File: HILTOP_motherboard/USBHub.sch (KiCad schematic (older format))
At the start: 64 parts, among them U2 TPS2044B, U3 TUSB2077A, U4 SN75240PWR, U6 SN75240PWR, Y1 6MHz Crystal

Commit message: Added new USB2.0 device
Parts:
- removed C28, C29, C36, C37, C38, C39, C40, C41, C42, C43, C44, C45, C46, C47, C48, C49: 22pF, Capacitors_SMD:C_0603, symbol C
- removed C31, C34: 100nF, Capacitors_SMD:C_0603, symbol C
- removed R18, R19, R23, R24, R29, R30, R34, R35, R36, R37, R40, R41, R42, R43, R46, R47: 27R, Resistors_SMD:R_0603, symbol R
- removed R22: 1.5K, Resistors_SMD:R_0603, symbol R
- removed R25, R26, R32, R33, R38, R39, R44, R45, R48, R49, R50, R51, R52, R53: 15K, Resistors_SMD:R_0603, symbol R
- removed R28, R31: 10K, Resistors_SMD:R_0603, symbol R
- removed U2: TPS2044B, Housings_SOIC:SOIC-16_3.9x9.9mm_Pitch1.27mm, symbol TPS2044B
- removed U3: TUSB2077A, Housings_QFP:LQFP-48_7x7mm_Pitch0.5mm, symbol TUSB2077A
- removed U4, U6: SN75240PWR, Housings_SSOP:TSSOP-8_4.4x3mm_Pitch0.65mm, symbol SN75240PWR
- added C? (x9): 100nF, Capacitors_SMD:C_0603, symbol C
- added C? (x4): 1uF, Capacitors_SMD:C_0603, symbol C
- added D? (x7): GRN, symbol LED
- added D? (x7): YEL, symbol LED
- added D? (x3): RED, symbol LED
- added R? (x6): 10K, Resistors_SMD:R_0603, symbol R
- added R? (x3): DNF, Resistors_SMD:R_0603, symbol R
- added R? (x17): 330R, Resistors_SMD:R_0603, symbol R
- added U3, U?: USB2517, MODULE, symbol USB2517
- added U? (x2): MIC2026-1YM, MODULE, symbol MIC2026-1YM
- C32: value 1nF -> 100nF; Devtank 106-004 -> 105-002
- R20: value 10K -> 100K; Devtank 101-010 -> 101-015
- R21: value 1.5K -> 1M; Devtank 101-032 -> 101-019
- R27: value 10K -> 12K; Devtank 101-010 -> 101-044
- Y1: value 6MHz Crystal -> 24MHz Crystal; Devtank 181-002 -> 181-003
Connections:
- net labels added: OCS1, OCS2, OCS4, PWR1_5V, PWR2_5V, PWR4_5V, USB1_EN, USB4_EN
- net labels removed: D2_5V, D3_5V, D6_5V, D7_5V, USB0_N, USB0_P, USB2_OC, USB3_EN, USB3_OC, USB6_EN, USB6_OC, USB7_EN, USB7_OC, USB_CFG_OK, USB_PORTDIS, USB_PORTPWR
- wire segments 240 -> 195
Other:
- note added: "Default Config - 101\nInternal Defaults\nDynamic Power (local)\nUSB LED Mode"
- note added: "Over-current Monitoring on external ports only"
- moved on the sheet: C30, C32, C33, C35, R152, R20, R21, R27, Y1

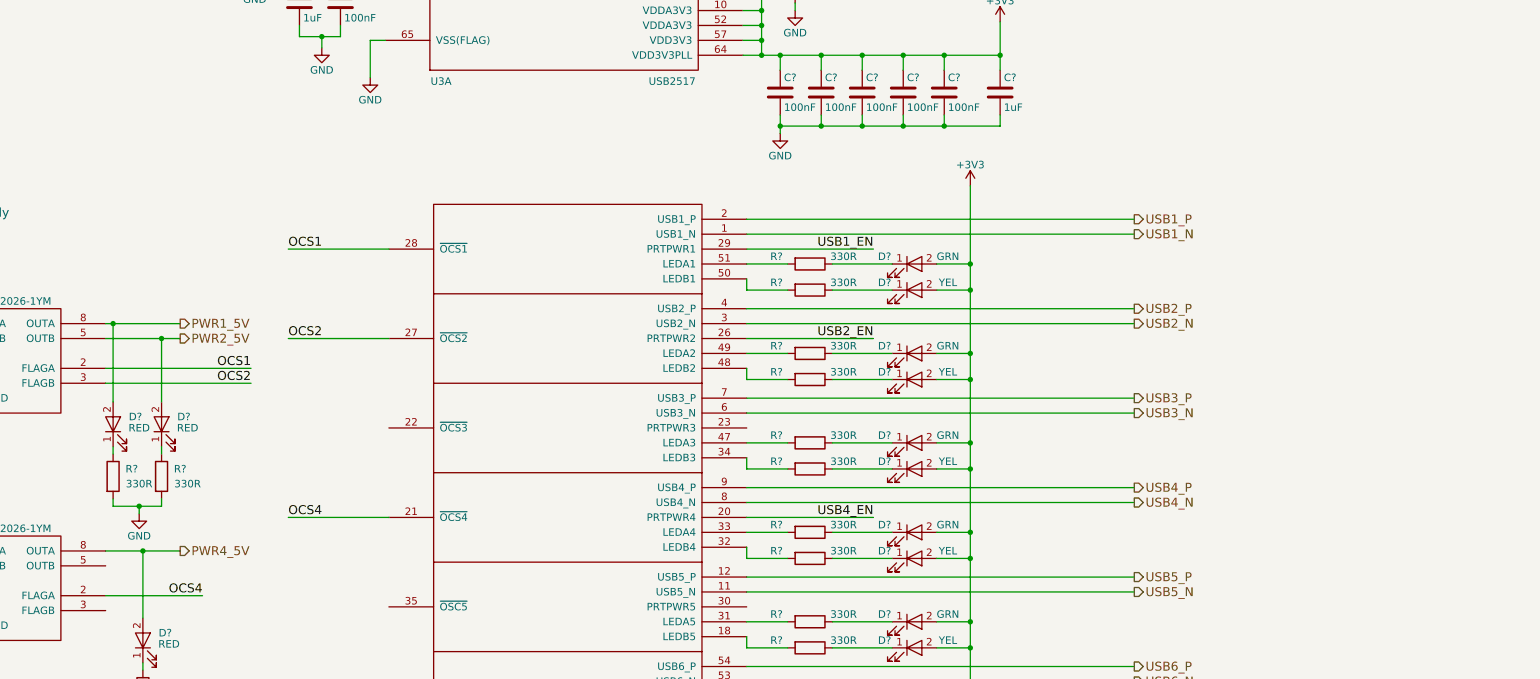
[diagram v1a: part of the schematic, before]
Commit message: add SP3003 ESD protection diodes to USB circuit
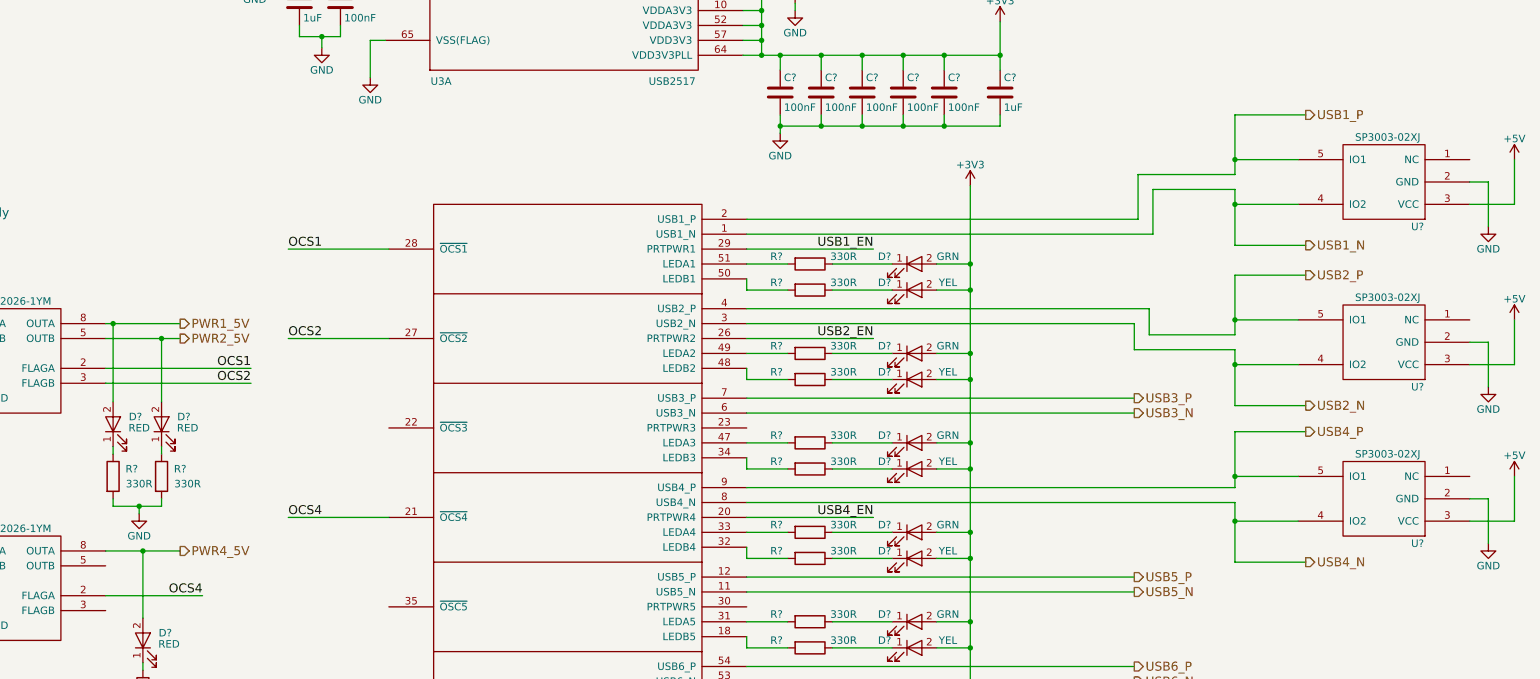
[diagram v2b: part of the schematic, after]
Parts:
- added U? (x3): SP3003-02XJ, Devtank_PCB_Lib:SC70-5, symbol SP3003-02XJ
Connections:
- net +5V: now also U?.3 (VCC), U?.3 (VCC), U?.3 (VCC)
- net GND: now also U?.2 (GND), U?.2 (GND), U?.2 (GND)
- net USB1_N: now also U?.4 (IO2)
- net USB1_P: now also U?.5 (IO1)
- net USB2_N: now also U?.4 (IO2)
- net USB2_P: now also U?.5 (IO1)
- net USB4_N: now also U?.4 (IO2)
- net USB4_P: now also U?.5 (IO1)

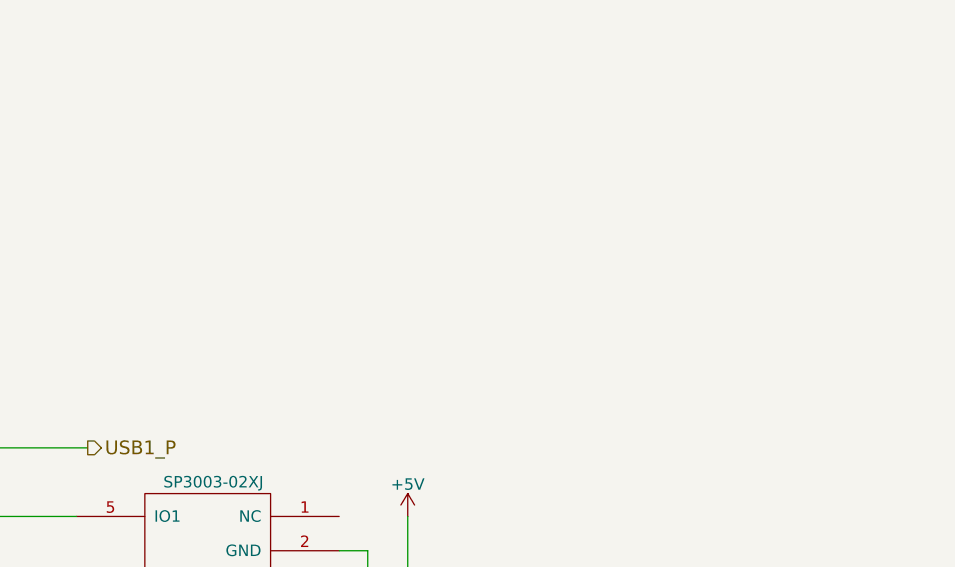
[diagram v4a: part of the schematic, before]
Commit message: Fixed giabit LAN Schematic errors
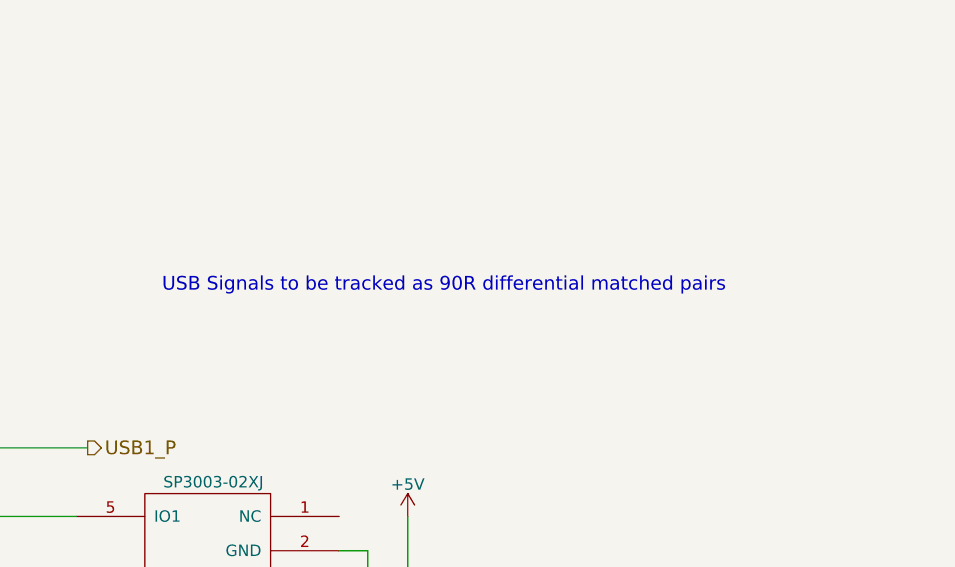
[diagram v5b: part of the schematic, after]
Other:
- note added: "USB Signals to be tracked as 90R differential matched pairs"
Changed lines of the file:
@@
 Wire Wire Line
 	12525 8100 12400 8100
+Text Notes 11625 4850 0    60   ~ 0
+USB Signals to be tracked as 90R differential matched pairs
 $EndSCHEMATC

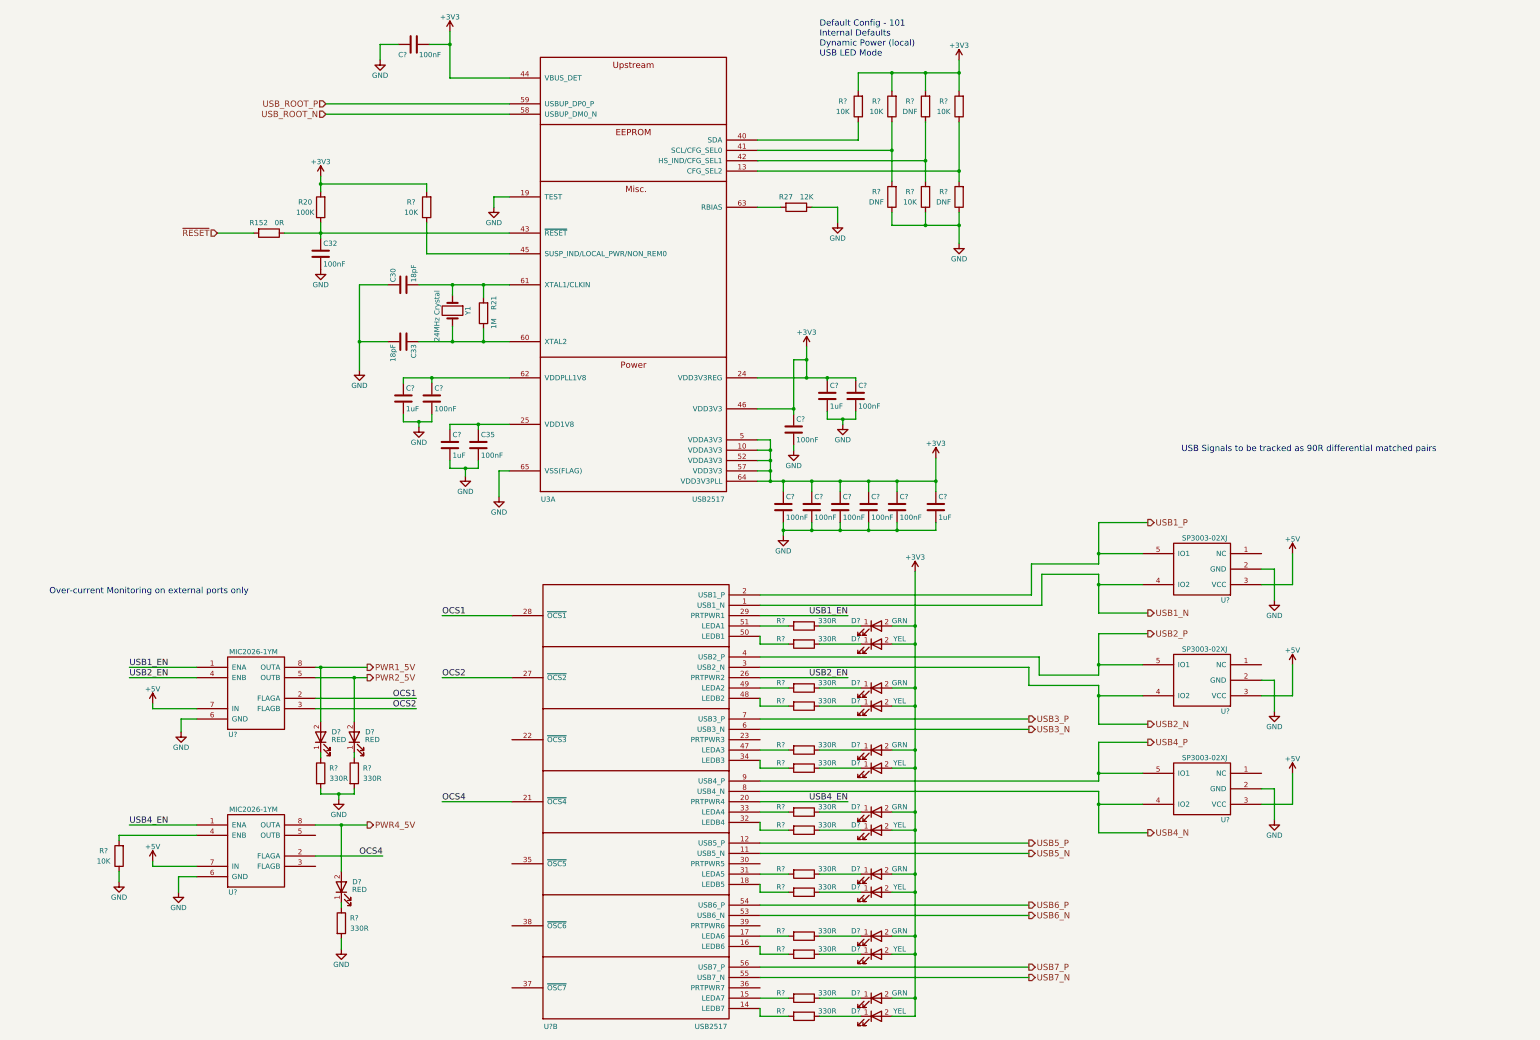
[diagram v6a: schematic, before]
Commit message: Furthe progress on Schematics, assigned all main footprints using latest libraries, removed unwanted tracking and parts from original PCB layout
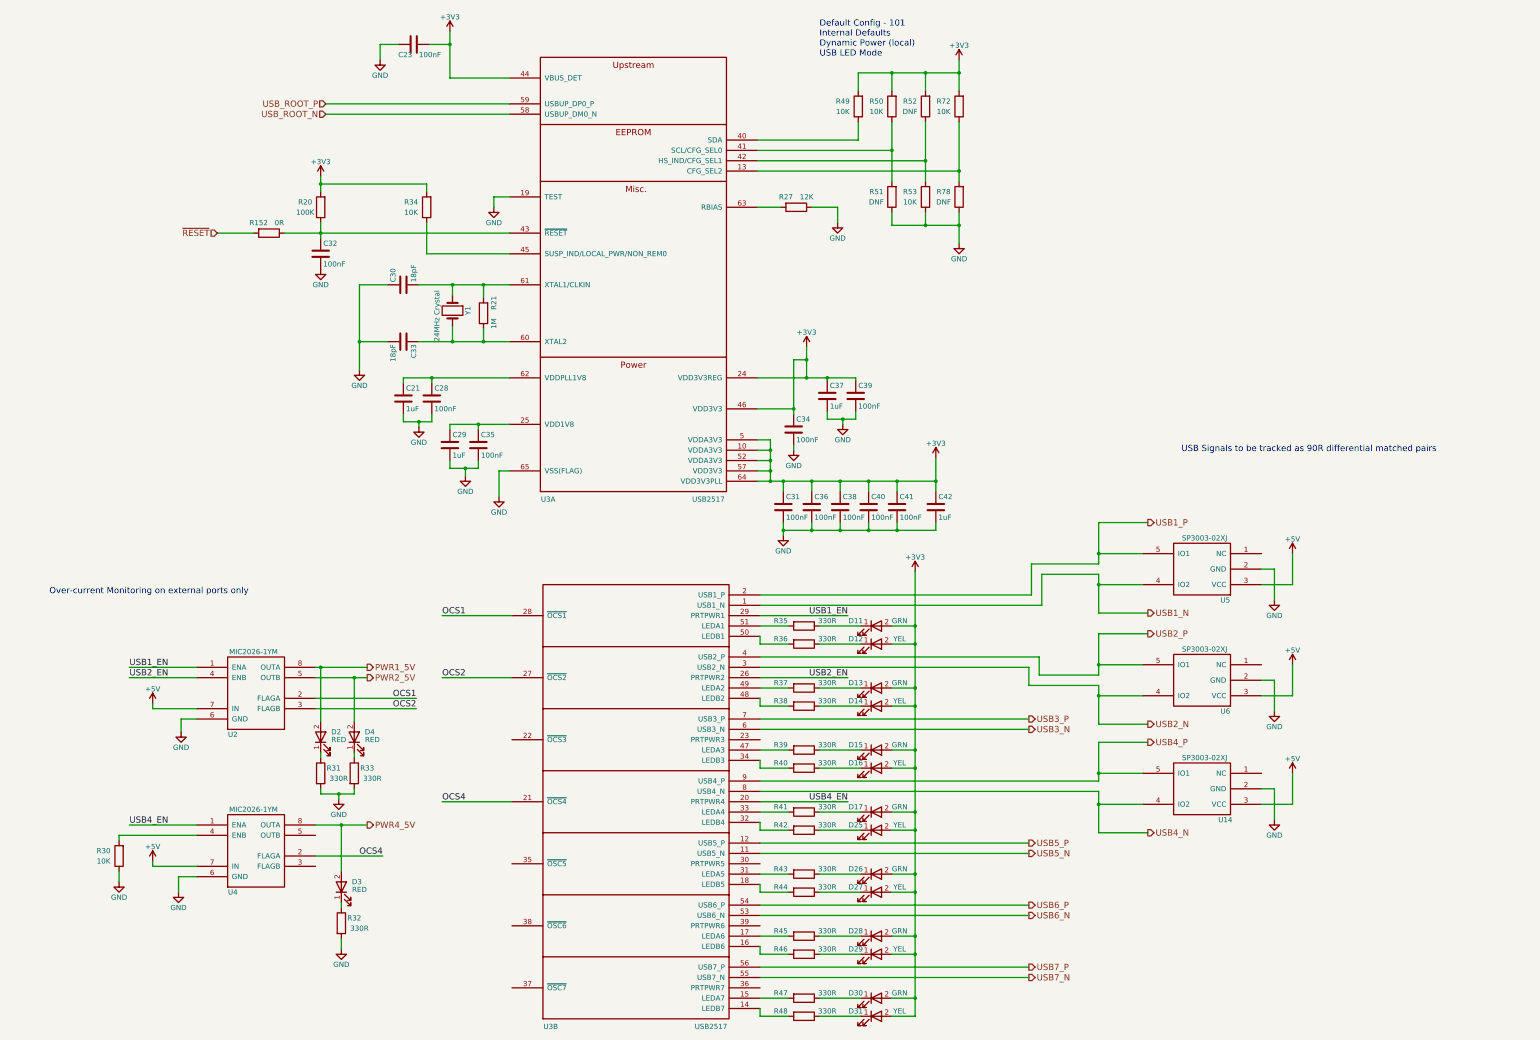
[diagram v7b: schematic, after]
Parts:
- C21, C23: renamed from C?; footprint Capacitors_SMD:C_0603 -> Capacitor_SMD:C_0603_1608Metric
- C28, C29, C31, C34, C36, C37, C38, C39, C40, C41, C42: renamed from C?; footprint Capacitors_SMD:C_0603 -> Capacitor_SMD:C_0201_0603Metric
- C30, C32, C33, C35: footprint Capacitors_SMD:C_0603 -> Capacitor_SMD:C_0201_0603Metric
- D11, D12, D13, D14, D15, D16, D17, D2, D25, D26, D27, D28, D29, D3, D30, D31, D4: renamed from D?; footprint (none) -> LED_SMD:LED_0603_1608Metric
- R152, R20, R21, R27: footprint Resistors_SMD:R_0603 -> Resistor_SMD:R_0603_1608Metric
- R30, R31, R32, R33, R34, R35, R36, R37, R38, R39, R40, R41, R42, R43, R44, R45, R46, R47, R48, R49, R50, R51, R52, R53, R72, R78: renamed from R?; footprint Resistors_SMD:R_0603 -> Resistor_SMD:R_0603_1608Metric
- U2, U4: renamed from U?; footprint MODULE -> Package_SOIC:SOIC-8_3.9x4.9mm_P1.27mm
- U3: footprint MODULE -> Devtank_PCB_Lib:QFN-64-1EP_9x9mm_P0.5mm_EP4.7x4.7mm
- U3: renamed from U?; footprint MODULE -> Package_DFN_QFN:QFN-64-1EP_9x9mm_P0.5mm
- Y1: footprint Crystals:Crystal_SMD_7050-2pin_7.0x5.0mm -> Crystal:Crystal_SMD_7050-2Pin_7.0x5.0mm
- gave numbers to parts that had none: 3

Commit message: Schematics complete - 1st draft
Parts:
- C21, C23, C28, C29, C30, C31, C32, C33, C34, C35, C36, C37, C38, C39, C40, C41, C42: symbol C -> device:C
- D11, D12, D13, D14, D15, D16, D17, D2, D25, D26, D27, D28, D29, D3, D30, D31, D4: symbol LED -> device:LED
- R152, R20, R21, R27, R30, R31, R32, R33, R34, R35, R36, R37, R38, R39, R40, R41, R42, R43, R44, R45, R46, R47, R48, R49, R50, R51, R52, R53, R72, R78: symbol R -> device:R
- U14, U5, U6: symbol SP3003-02XJ -> Devtank:SP3003-02XJ
- U2, U4: symbol MIC2026-1YM -> Devtank:MIC2026-1YM
- U3: symbol USB2517 -> Devtank:USB2517
- U3: footprint Package_DFN_QFN:QFN-64-1EP_9x9mm_P0.5mm -> Devtank_PCB_Lib:QFN-64-1EP_9x9mm_P0.5mm_EP4.7x4.7mm; symbol USB2517 -> Devtank:USB2517
- Y1: symbol Crystal -> device:Crystal
